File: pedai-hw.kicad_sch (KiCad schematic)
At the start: 8 parts, among them J15 Spare_ADC, J16 left_connector_blackpill, J17 right_connector_blackpill, J3 I2S_module, J4 Unused_pins_I2S, J5 LCD1602a

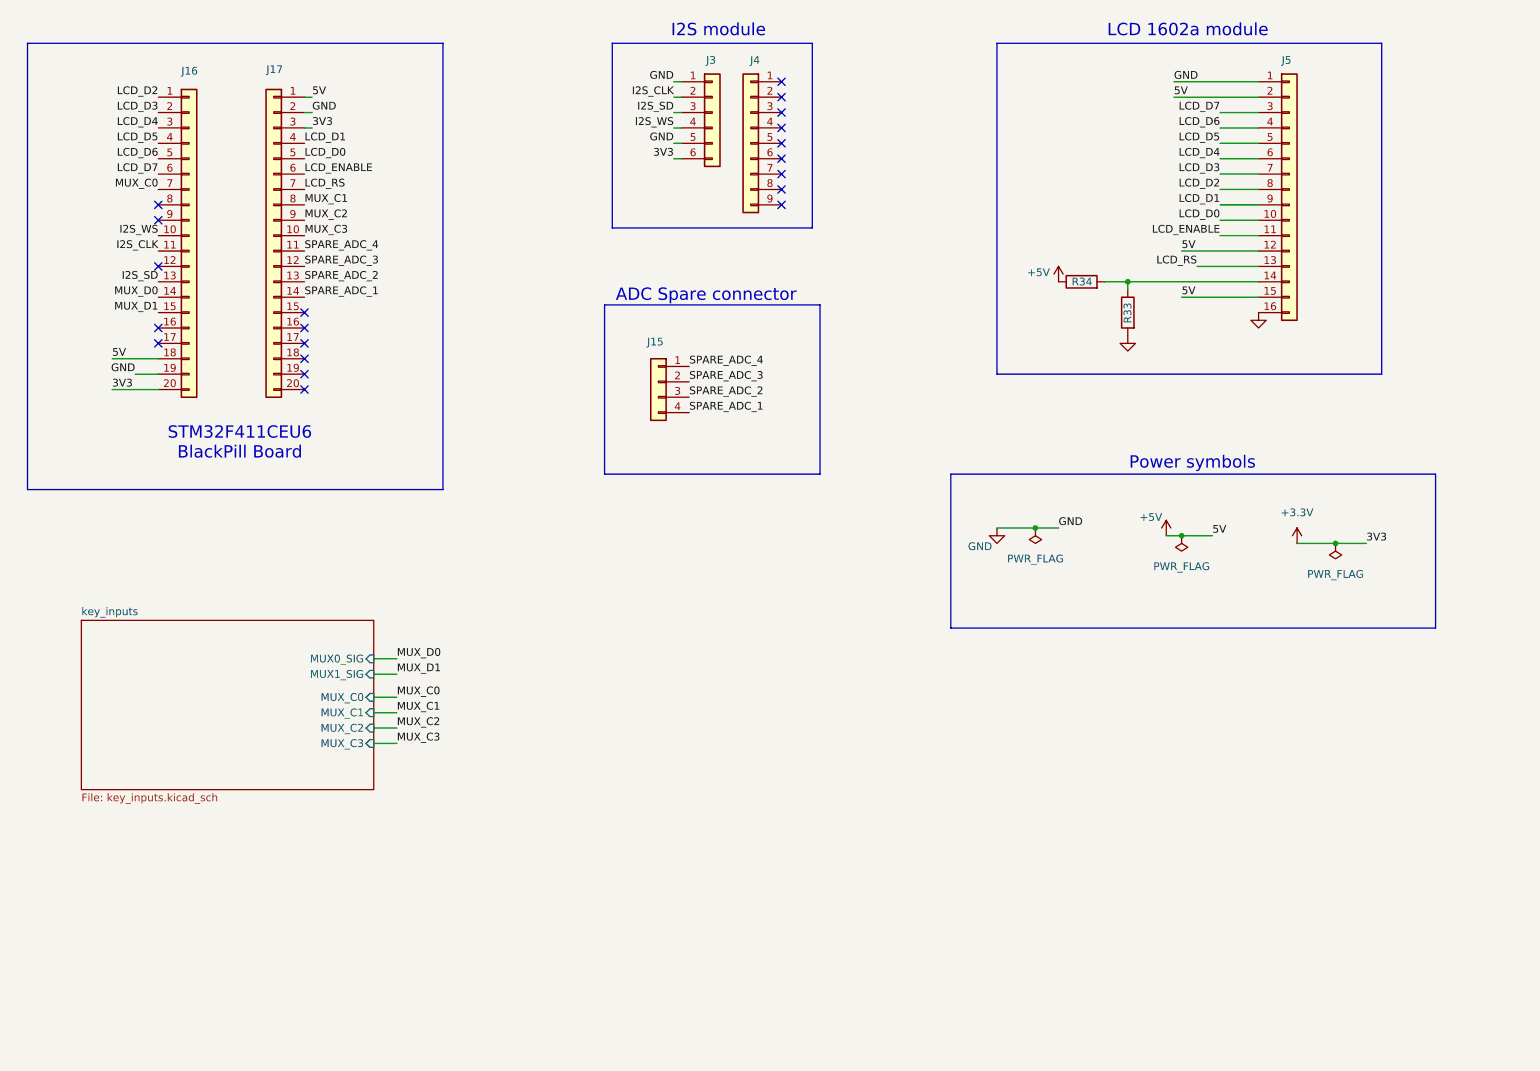
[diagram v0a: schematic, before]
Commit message: fix: replaced 16 channel mux modules with 8 channels mux chips schematic concluded and added 3d models
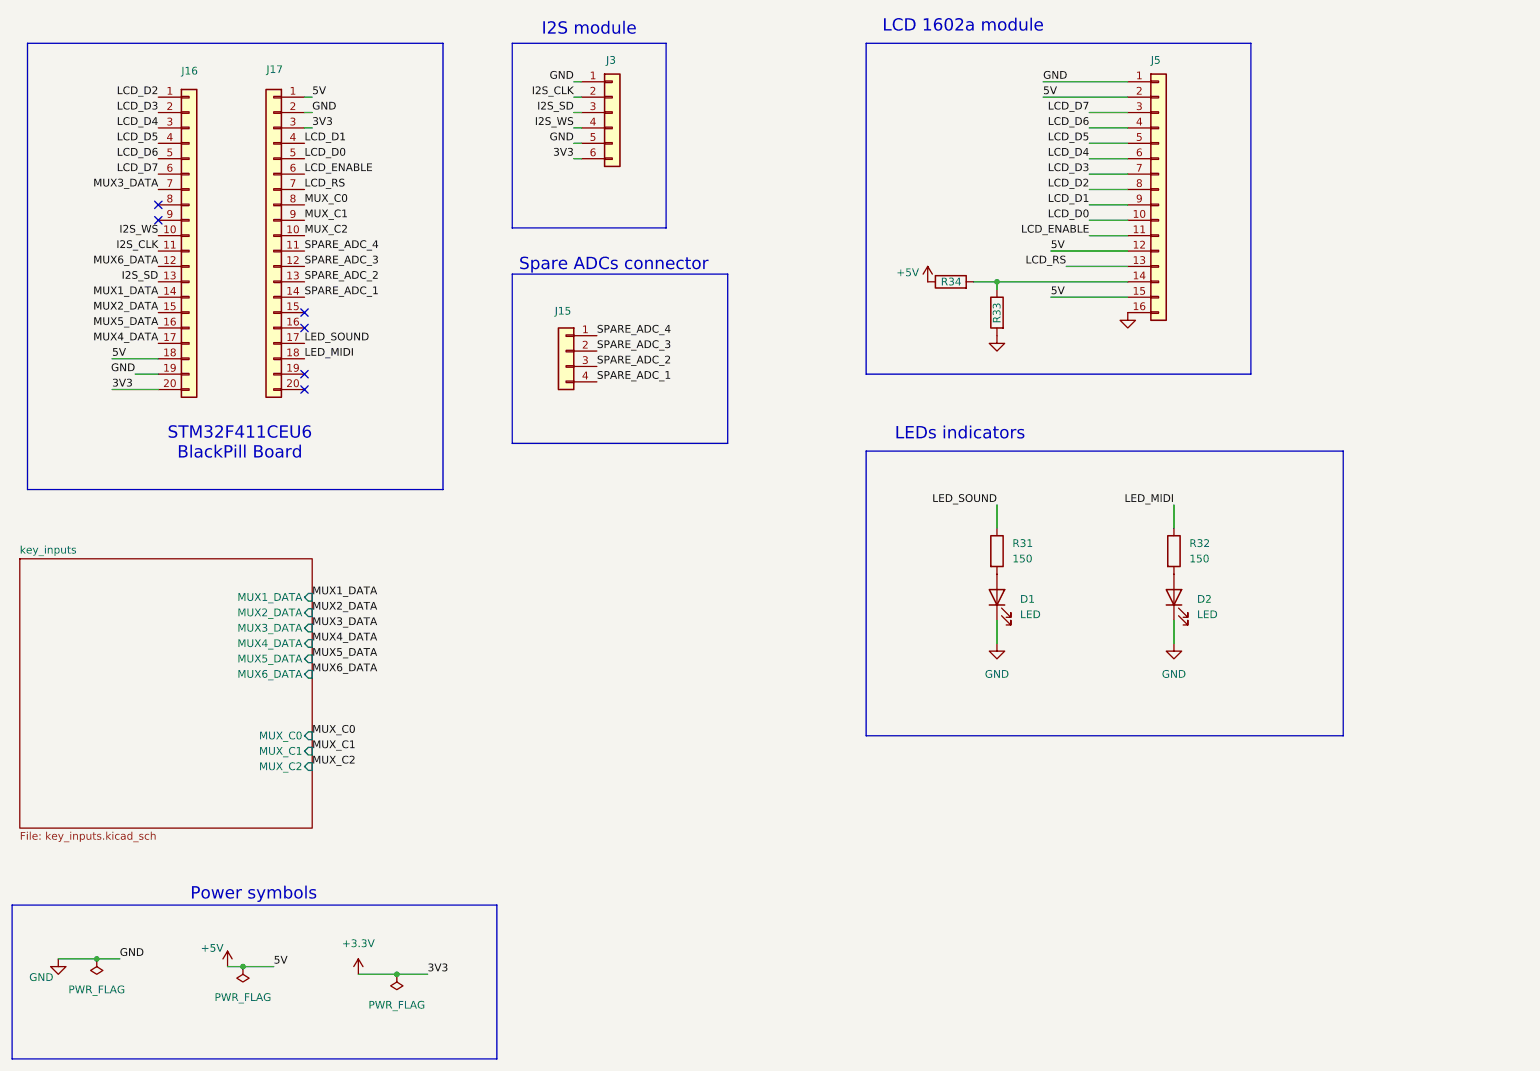
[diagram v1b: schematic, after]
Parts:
- removed J4: Unused_pins_I2S, Connector_PinSocket_2.54mm:PinSocket_1x09_P2.54mm_Vertical, symbol Connector_Generic:Conn_01x09
- added D1, D2: LED, LED_THT:LED_D3.0mm, symbol Device:LED
- added R31, R32: 150, Resistor_THT:R_Axial_DIN0204_L3.6mm_D1.6mm_P5.08mm_Vertical, symbol Device:R
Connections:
- net MUX_C3 is gone; now on net MUX_C2: J17.10 (Pin_10)
- net GND: now also D1.1 (K), D2.1 (K)
- net MUX_C0: now also J17.8 (Pin_8); no longer J16.7 (Pin_7)
- net MUX_C1: now also J17.9 (Pin_9); no longer J17.8 (Pin_8)
- net MUX_C2: no longer J17.9 (Pin_9)
- net LED_SOUND: now reaches J17.17 (Pin_17)
- net LED_SOUND: now also R31.1
- net LED_MIDI: now reaches J17.18 (Pin_18)
- net LED_MIDI: now also R32.1
- net MUX6_DATA: now reaches J16.12 (Pin_12)
- net MUX5_DATA: now reaches J16.16 (Pin_16)
- net MUX4_DATA: now reaches J16.17 (Pin_17)
- net MUX_D0 renamed MUX1_DATA
- net MUX_D1 renamed MUX2_DATA
- new net: D1.2 (A), R31.2
- new net: D2.2 (A), R32.2
- new net MUX3_DATA: J16.7 (Pin_7)
- no-connect marks 20 -> 6
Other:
- sheet key_inputs ports: added MUX1_DATA, MUX2_DATA, MUX3_DATA, MUX4_DATA, MUX5_DATA, MUX6_DATA; removed MUX0_SIG, MUX1_SIG, MUX_C3
- note added: "LEDs indicators"
- note added: "Spare ADCs connector"
- note removed: "ADC Spare connector"
- moved on the sheet: J15, J3, J5, R33, R34

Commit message: layout and routing finished
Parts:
- added H1, H2, H3, H4: MountingHole, MountingHole:MountingHole_4.3mm_M4, symbol Mechanical:MountingHole
- R31, R32, R33, R34: footprint Resistor_THT:R_Axial_DIN0204_L3.6mm_D1.6mm_P5.08mm_Vertical -> Resistor_THT:R_Axial_DIN0204_L3.6mm_D1.6mm_P5.08mm_Horizontal
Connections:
- net +5V: no longer J17.1 (Pin_1)
- no-connect marks 6 -> 7
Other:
- note added: "Mounting Holes"

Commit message: fabrication output, silkscreen
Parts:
- removed H3, H4: MountingHole, MountingHole:MountingHole_4.3mm_M4, symbol Mechanical:MountingHole
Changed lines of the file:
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@@
 	(rectangle
 		(start 109.22 99.06)
-		(end 156.21 120.65)
+		(end 156.21 111.76)
 		(stroke
 			(width 0)
@@
 				(path "/b6e54648-49ac-4cc8-aea0-d315d4d08ac8"
 					(reference "#PWR032")
-					(unit 1)
-				)
-			)
-		)
-	)
-	(symbol
-		(lib_id "Mechanical:MountingHole")
-		(at 115.57 114.3 0)
-		(unit 1)
-		(exclude_from_sim yes)
-		(in_bom no)
-		(on_board yes)
-		(dnp no)
-		(fields_autoplaced yes)
-		(property "Reference" "H3"
-			(at 118.11 113.0299 0)
-			(effects
-				(font
-					(size 1.27 1.27)
-				)
-				(justify left)
-			)
-		)
-		(property "Value" "MountingHole"
-			(at 118.11 115.5699 0)
-			(effects
-				(font
-					(size 1.27 1.27)
-				)
-				(justify left)
-			)
-		)
-		(property "Footprint" "MountingHole:MountingHole_4.3mm_M4"
-			(at 115.57 114.3 0)
-			(effects
-				(font
-					(size 1.27 1.27)
-				)
-				(hide yes)
-			)
-		)
-		(property "Datasheet" "~"
-			(at 115.57 114.3 0)
-			(effects
-				(font
-					(size 1.27 1.27)
-				)
-				(hide yes)
-			)
-		)
-		(property "Description" "Mounting Hole without connection"
-			(at 115.57 114.3 0)
-			(effects
-				(font
-					(size 1.27 1.27)
-				)
-				(hide yes)
-			)
-		)
-		(instances
-			(project "pedai-hw"
-				(path "/b6e54648-49ac-4cc8-aea0-d315d4d08ac8"
-					(reference "H3")
 					(unit 1)
 				)
@@
 					(unit 1)
 				)
-			)
-		)
-	)
-	(symbol
-		(lib_id "Mechanical:MountingHole")
-		(at 135.89 114.3 0)
-		(unit 1)
-		(exclude_from_sim yes)
-		(in_bom no)
-		(on_board yes)
-		(dnp no)
-		(fields_autoplaced yes)
-		(property "Reference" "H4"
-			(at 138.43 113.0299 0)
-			(effects
-				(font
-					(size 1.27 1.27)
-				)
-				(justify left)
-			)
-		)
-		(property "Value" "MountingHole"
-			(at 138.43 115.5699 0)
-			(effects
-				(font
-					(size 1.27 1.27)
-				)
-				(justify left)
-			)
-		)
-		(property "Footprint" "MountingHole:MountingHole_4.3mm_M4"
-			(at 135.89 114.3 0)
-			(effects
-				(font
-					(size 1.27 1.27)
-				)
-				(hide yes)
-			)
-		)
-		(property "Datasheet" "~"
-			(at 135.89 114.3 0)
-			(effects
-				(font
-					(size 1.27 1.27)
-				)
-				(hide yes)
-			)
-		)
-		(property "Description" "Mounting Hole without connection"
-			(at 135.89 114.3 0)
-			(effects
-				(font
-					(size 1.27 1.27)
-				)
-				(hide yes)
-			)
-		)
-		(instances
-			(project "pedai-hw"
-				(path "/b6e54648-49ac-4cc8-aea0-d315d4d08ac8"
-					(reference "H4")
-					(unit 1)
-				)

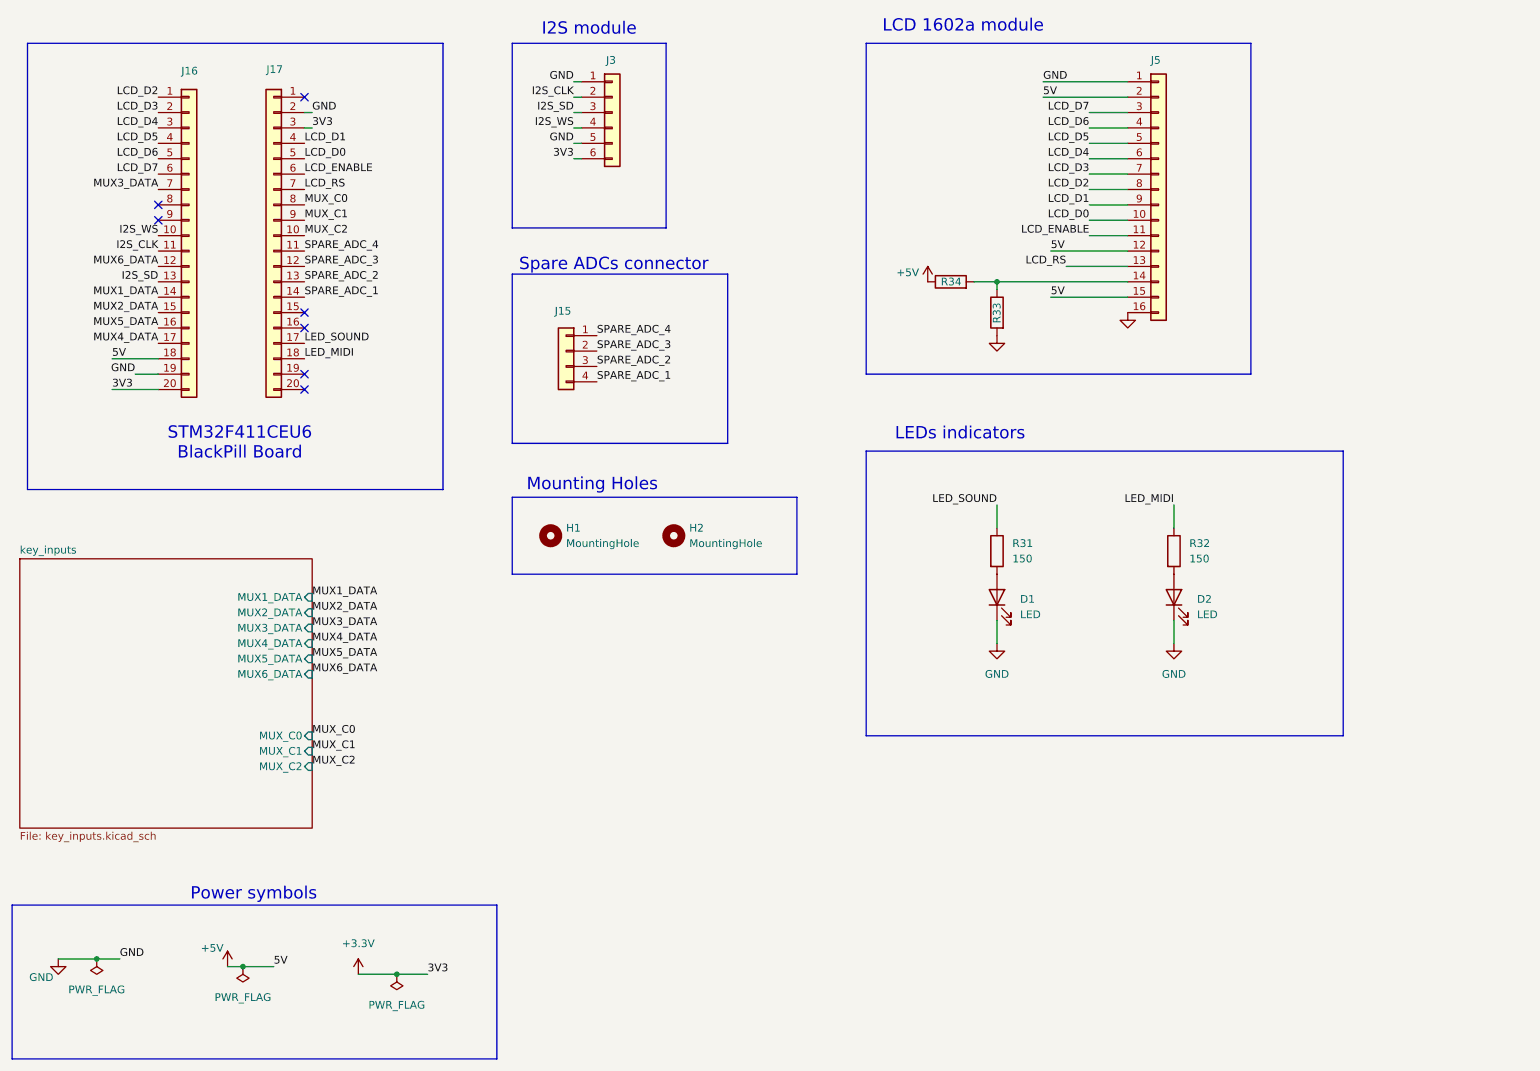
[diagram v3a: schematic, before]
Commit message: VERSION 0.9 ready for production silkscreen meme and not meme, ground pad, potentiometer for volume control and switch to turn off the device
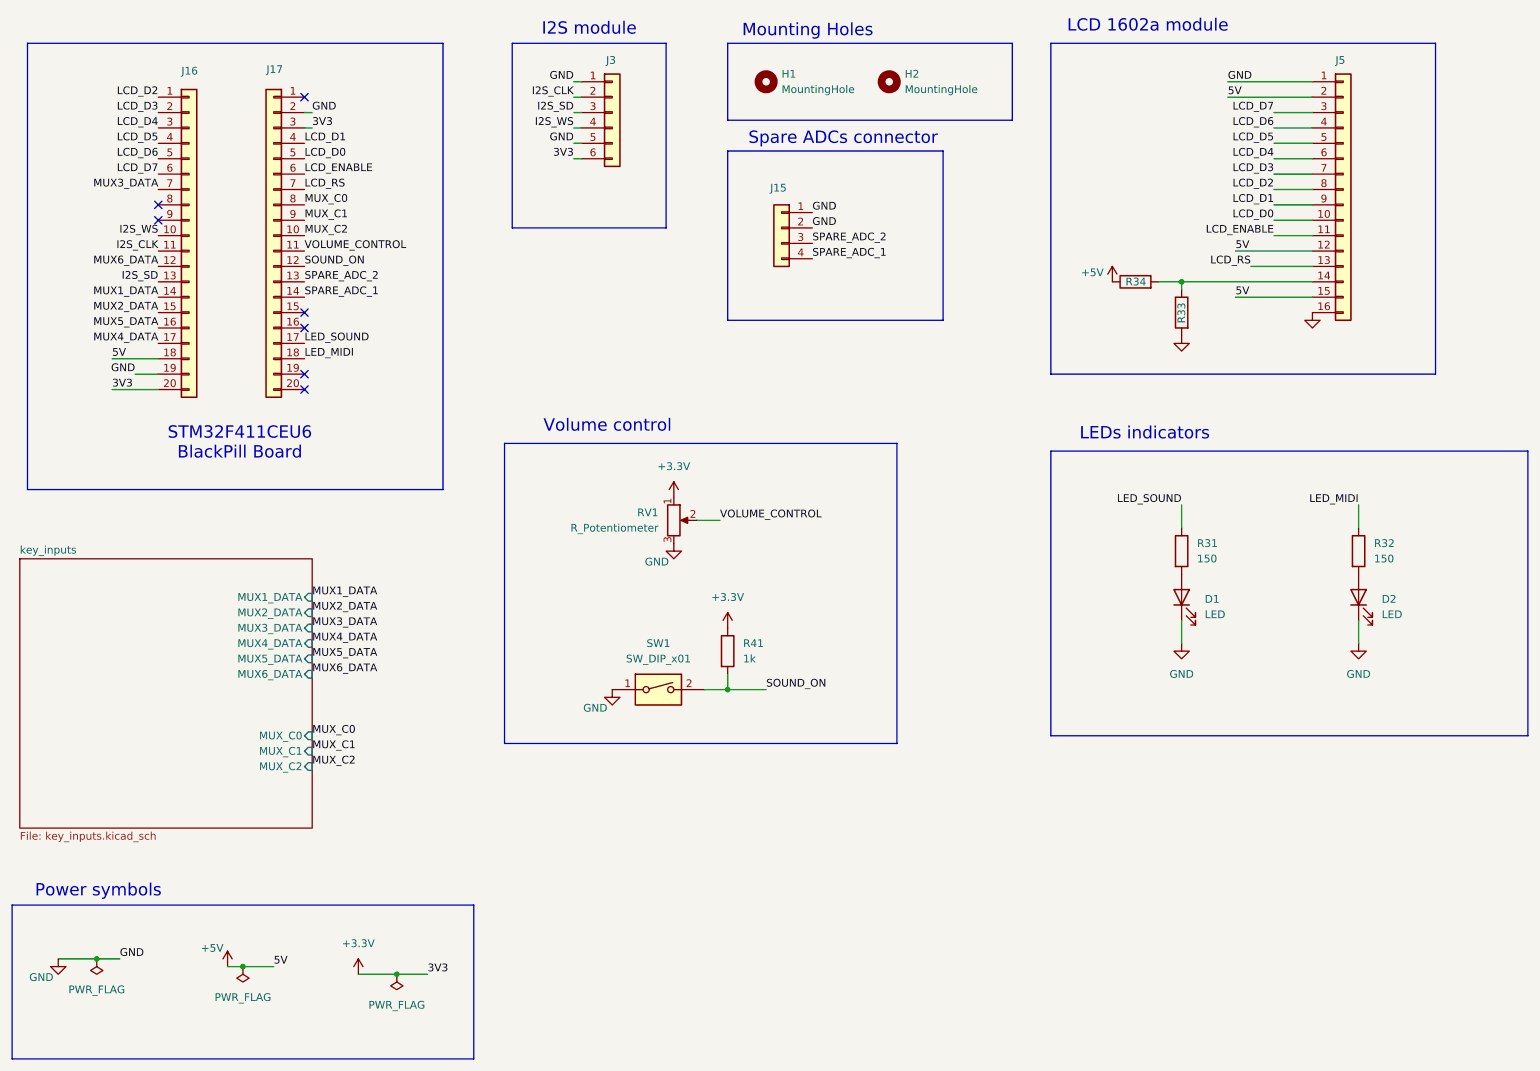
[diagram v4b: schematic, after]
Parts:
- added R41: 1k, Resistor_THT:R_Axial_DIN0204_L3.6mm_D1.6mm_P5.08mm_Horizontal, symbol Device:R
- added RV1: R_Potentiometer, Potentiometer_THT:Potentiometer_Alps_RK163_Single_Horizontal, symbol Device:R_Potentiometer
- added SW1: SW_DIP_x01, Library:KCD1-101, symbol Switch:SW_DIP_x01
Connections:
- net +3.3V: now also R41.1, RV1.1
- net GND: now also J15.1 (Pin_1), J15.2 (Pin_2), RV1.3, SW1.1
- net SPARE_ADC_3 renamed SOUND_ON
- net SOUND_ON: now also R41.2, SW1.2; no longer J15.2 (Pin_2)
- net SPARE_ADC_4 renamed VOLUME_CONTROL
- net VOLUME_CONTROL: now also RV1.2; no longer J15.1 (Pin_1)
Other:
- note added: "Volume control"
- moved on the sheet: D1, D2, H1, H2, J15, J5, R31, R32, R33, R34

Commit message: BREAKING: production
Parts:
- added C7: 100n, Capacitor_THT:CP_Radial_D4.0mm_P2.00mm, symbol Device:C
- added J11: Conn_01x09, Connector_PinSocket_2.54mm:PinSocket_1x09_P2.54mm_Vertical, symbol Connector_Generic:Conn_01x09
- added J2: Ground connector 1, Connector_PinHeader_2.54mm:PinHeader_1x04_P2.54mm_Vertical, symbol Connector:Conn_01x04_Pin
- added J4: Ground connector 2, Connector_PinHeader_2.54mm:PinHeader_1x04_P2.54mm_Vertical, symbol Connector:Conn_01x04_Pin
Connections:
- net +5V: now also C7.1; no longer J5.12 (Pin_12)
- net GND: now also J5.12 (Pin_12), C7.2, J2.1 (Pin_1), J2.2 (Pin_2), J2.3 (Pin_3), J2.4 (Pin_4), J4.1 (Pin_1), J4.2 (Pin_2), J4.3 (Pin_3), J4.4 (Pin_4)
- no-connect marks 7 -> 16
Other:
- note added: "Ground connectors for keys"
